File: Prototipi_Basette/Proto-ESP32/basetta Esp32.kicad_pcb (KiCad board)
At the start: 2 copper layers, 76.6 x 67.3 mm, 33 parts, among them J1 Conn_01x19, J2 Conn_01x19, J3 Conn_01x19, J4 Conn_01x19, J5 Screw_Terminal_01x02, J6 Conn_01x05, J7 Conn_01x02, J8 Conn_01x05, J9 Conn_01x05, Q1 BC547, Q2 BC547, Q3 IRF9540N, Q4 BC547, Q5 BC557, SW1 RESET, SW2 SET, U3 4013

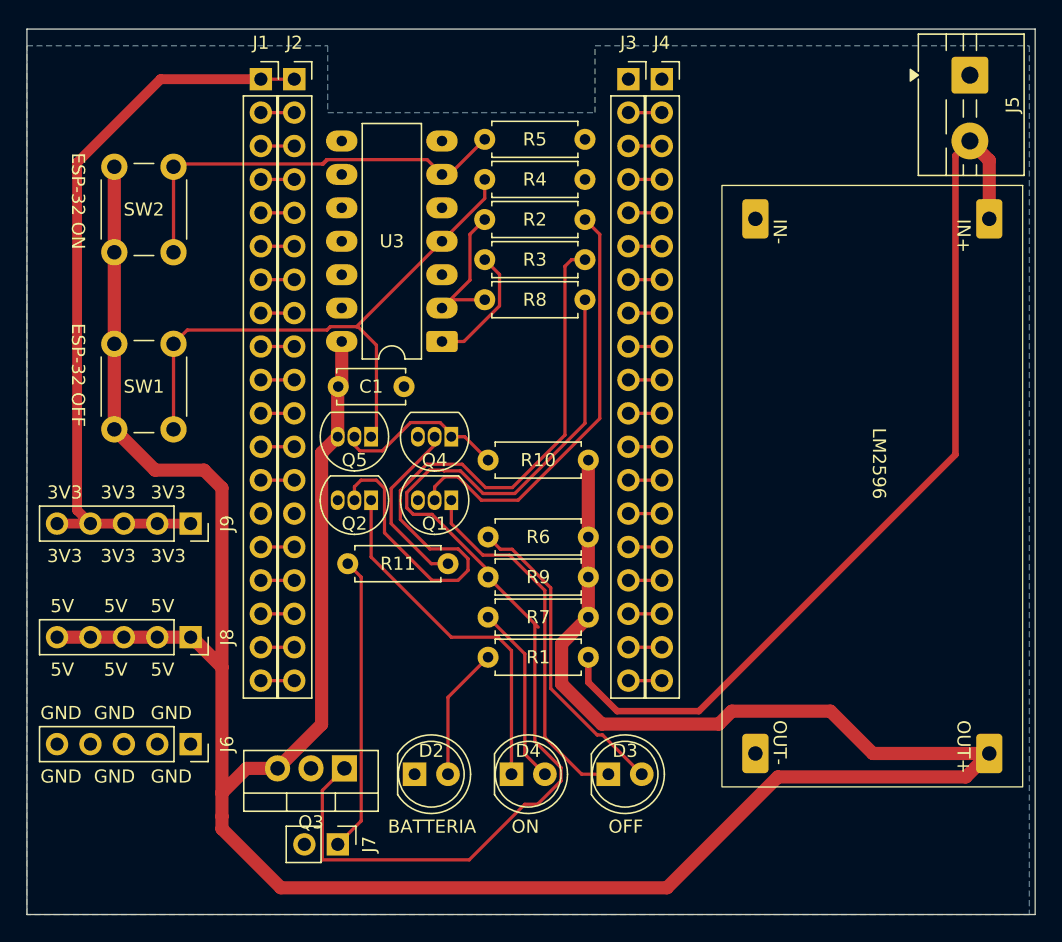
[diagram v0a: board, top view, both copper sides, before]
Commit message: Adjust PCB footprints, pads and routing
Move and reorient multiple footprints and update PCB geometry/metadata for the Proto-ESP32 layout. Changes include repositioning several resistors, TO-92 transistors, LEDs and a pin header; adding/adjusting pad rotation attributes (thru-hole pads set to 180 where needed); reordering and correcting silkscreen/fab lines and arcs; updating many footprint element UUIDs; and modifying F.Cu trace segments (notably for the +5V net) to match the new component placements. Also updated related project files and removed the KiCad .lck file.
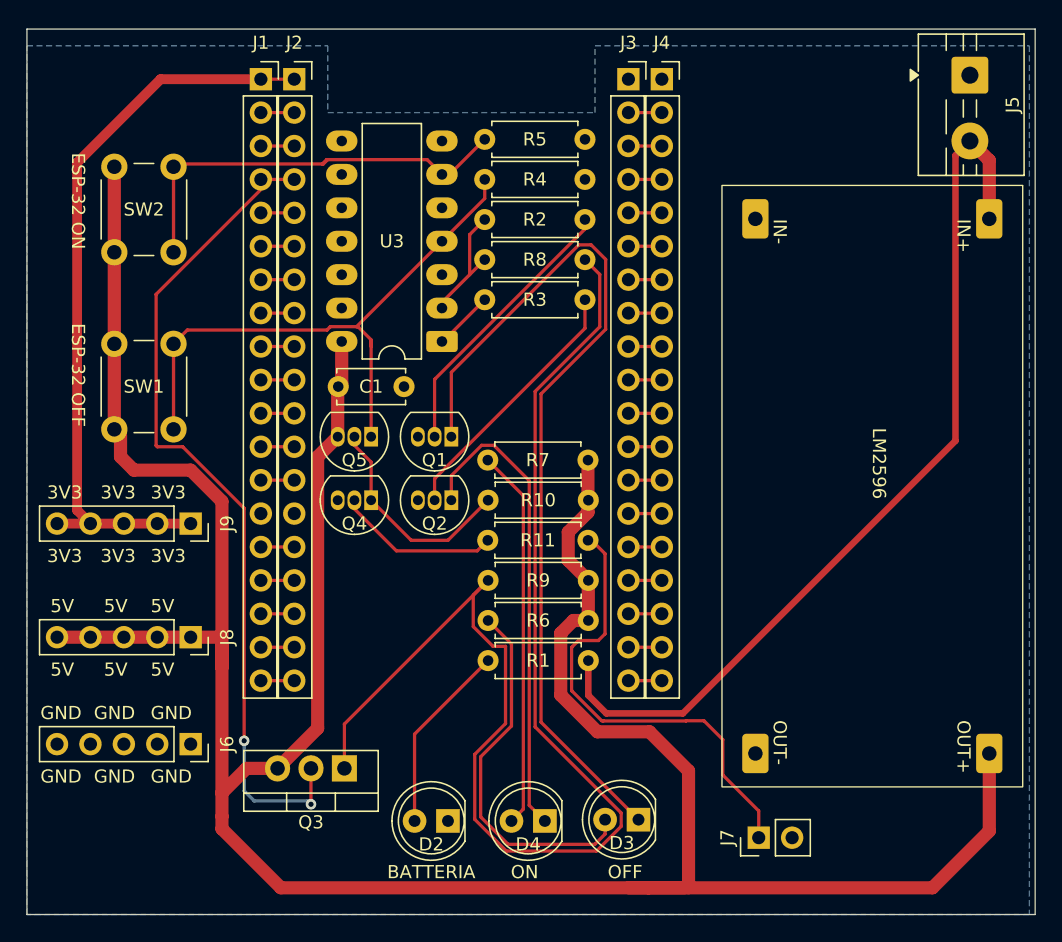
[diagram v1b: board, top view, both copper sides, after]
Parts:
- moved J7 32.0 mm to (177.5, 118.6), turned to 90 degrees
- moved R11 18.3 mm to (164.6, 96.0), turned to 180 degrees
- moved R7 11.9 mm to (164.6, 89.9)
- moved Q4 7.78 mm to (148.1, 93.0)
- moved R6 6.35 mm to (164.6, 102.1)
- moved Q2 6.10 mm to (154.2, 93.0)
- moved Q1 4.83 mm to (154.2, 88.1)
- moved D2 4.37 mm to (153.9, 117.3), turned to 180 degrees
- moved D4 4.37 mm to (161.3, 117.3), turned to 180 degrees
- moved D3 4.15 mm to (168.4, 117.2), turned to 180 degrees
- moved R10 3.05 mm to (164.6, 93.0)
- moved R3 3.05 mm to (156.7, 77.7)
- moved R8 3.05 mm to (156.7, 74.7)
- moved R1 0.25 mm to (164.6, 105.2)
- moved R9 0.25 mm to (157.0, 99.1)
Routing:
- net ESP-32 POW: track 2.54 -> 64.5 mm, vias 0 -> 2
- net Net-(D3-K): track 28.2 -> 69.0 mm
- net Net-(Q2-B): track 55.1 -> 20.0 mm
- net Net-(Q3-G): track 82.8 -> 101.2 mm
- net Net-(D4-A): track 13.7 -> 28.9 mm
- net Net-(J7-Pin_1): track 22.5 -> 35.7 mm
- net Net-(Q1-B): track 32.8 -> 21.9 mm
- net Net-(D4-K): track 27.3 -> 36.2 mm
- net +5V: track 228.5 -> 223.5 mm
- net Net-(U3A-Q): track 9.48 -> 4.57 mm
- net Net-(D3-A): track 23.6 -> 28.4 mm
- net Net-(D2-A): track 10.2 -> 14.5 mm
- net Net-(Q4-C): track 13.2 -> 16.8 mm
- net Net-(Q4-B): track 13.6 -> 12.4 mm
- net SIGN_ESP32: track 11.6 -> 10.6 mm

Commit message: Update MOSFET footprint, nets and refs
Modify PCB to replace a TO-92 footprint with a TO-220 horizontal power MOSFET (IRF9540N) and update related component properties, 3D model and datasheet. Fix pad nets (Q3-G -> Q6-G), adjust component placement (button Y pos), add units block to sheet instance, and update many footprint geometry, silk/fab/crtyd outlines and UUIDs. .kicad_pcb (and associated project files) updated to reflect new pad sizes, drills, pad ordering and property metadata for Q4/Q5/Q6 and related footprints.
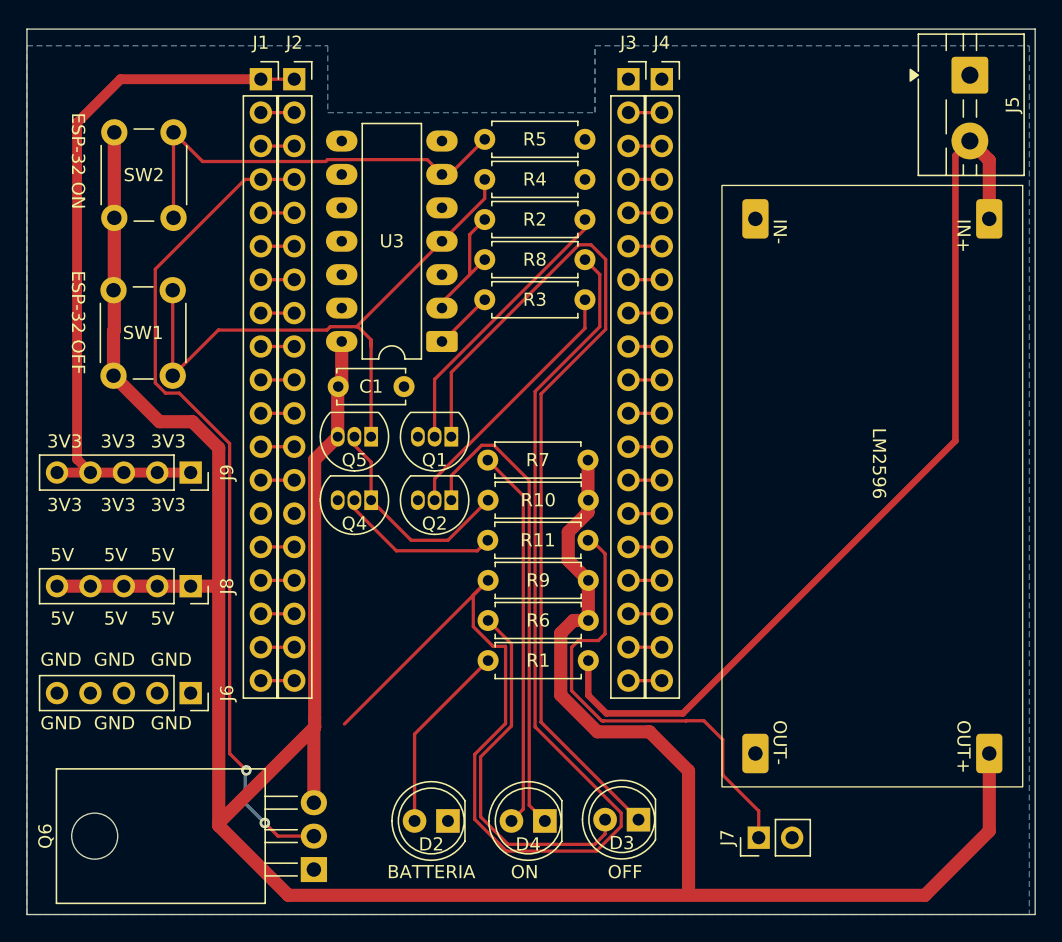
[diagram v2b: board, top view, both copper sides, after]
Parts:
- removed Q3: IRF9540N, Package_TO_SOT_THT:TO-220-3_Vertical
- added Q6: IRF9540N, Package_TO_SOT_THT:TO-220-3_Horizontal_TabDown, F.Cu at (143.7, 121.0)
- R11: value R -> 2.2k
- moved SW1 4.08 mm to (128.5, 83.5)
- moved J6 3.88 mm to (134.4, 107.6)
- moved J8 3.88 mm to (134.4, 99.5)
- moved J9 3.88 mm to (134.4, 90.9)
- moved SW2 2.62 mm to (128.6, 71.5)
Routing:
- net Net-(Q6-G): track 101.2 -> 97.8 mm
- net +5V: track 223.5 -> 226.7 mm
- net +3V3: track 57.9 -> 55.8 mm
- net Suicide: track 45.6 -> 46.6 mm
- net ESP-32 POW: track 64.5 -> 63.8 mm

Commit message: Add mounting holes and tidy PCB footprints
Added two M3 mounting-hole footprints and multiple thru-hole pads (GND connected). Cleaned up many footprints by hiding F.Fab value/reference texts, removing redundant fp_text user elements, and adjusting reference designators (several Q/R/J renames). Updated component positions (connectors/terminal block), fixed net assignments for several pads/nets, and refreshed UUIDs across footprints. Overall PCB housekeeping and footprint consistency updates.
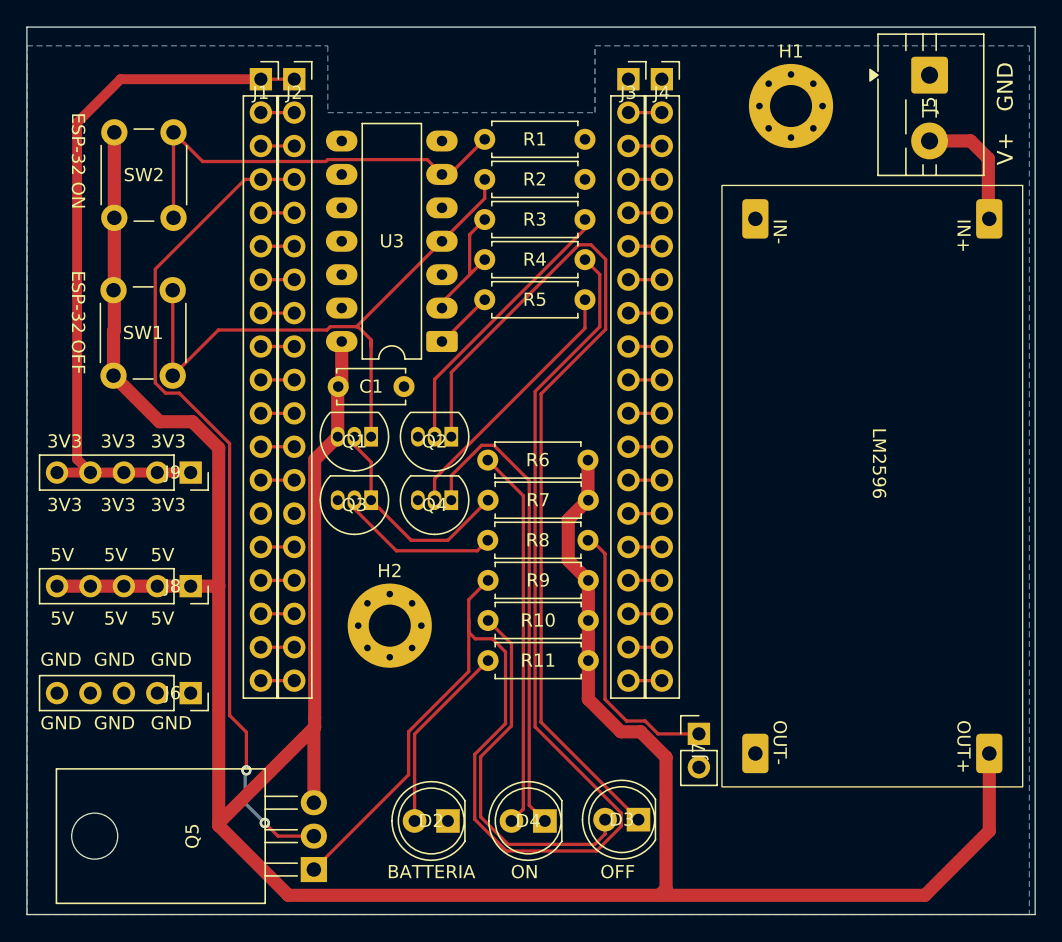
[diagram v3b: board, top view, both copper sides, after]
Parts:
- added H1: MountingHole_Pad, MountingHole:MountingHole_3.2mm_M3_Pad_Via, F.Cu at (180.0, 63.0)
- added H2: MountingHole_Pad, MountingHole:MountingHole_3.2mm_M3_Pad_Via, F.Cu at (149.5, 102.5)
- R11: renamed from R1; value R -> 1k
- moved J7 9.11 mm to (173.0, 110.7), turned to 0 degrees
- moved J5 3.07 mm to (190.5, 60.7)
- renumbered Q5 to Q1, Q1 to Q2, Q4 to Q3, Q2 to Q4, Q6 to Q5, R5 to R1, R6 to R10, R4 to R2, R2 to R3, R8 to R4, R3 to R5, R7 to R6, R10 to R7, R11 to R8
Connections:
- R11 pad 1: V_in_Batterie -> +5V
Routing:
- net V_in_Batterie: track 69.5 -> 9.68 mm
- net Net-(J7-Pin_1): track 35.7 -> 21.0 mm
- net Net-(Q5-G): track 97.8 -> 106.8 mm
- net +5V: track 226.7 -> 222.9 mm
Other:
- board size 76.6 x 67.3 mm -> 76.6 x 67.5 mm
- board text added: "V+ GND"
